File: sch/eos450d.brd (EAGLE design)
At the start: 100 x 80 mm, 19 parts, among them IC1 ATTINY13V, IC2 74HC595, Q1 MMBT2222

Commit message: Schematic complete. Added Gerber files
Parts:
- removed IC1: ATTINY13V, SparkFun-DigitalIC:SO08
- added ISP1: AVRISP-6, adafruit:AVRISP
- added U1: Tiny45-20-SMT, SparkFun-DigitalIC:SO08-EIAJ
- R1, R2: value 51 -> 330
- R3, R4: value 5.6k -> 10k
- R5: value 4.7k -> 3.3k
- R6: value 100 -> 180
- moved C1 80.5 mm to (9.61, 6.53), turned to 90 degrees
- moved R3 69.1 mm to (15.9, 12.1), turned to 180 degrees
- moved R5 67.8 mm to (16.9, 25.9), flipped to the bottom, turned to 90 degrees
- moved S1 67.3 mm to (15.8, 4.99), turned to 90 degrees
- moved C3 65.9 mm to (15.9, 10.1), turned to 180 degrees
- moved S2 64.8 mm to (3.56, 5.08), turned to 270 degrees
- moved C5 64.4 mm to (3.76, 29.5), flipped to the bottom, turned to 90 degrees
- moved R4 63.2 mm to (3.48, 12.1)
- moved Q1 62.7 mm to (16.0, 31.5), flipped to the bottom
- moved C4 61.8 mm to (3.50, 10.1)
- moved R6 55.3 mm to (9.54, 60.1), flipped to the bottom, turned to 180 degrees
- moved R1 52.4 mm to (2.99, 41.1), flipped to the bottom, turned to 180 degrees
- moved D2 47.6 mm to (9.61, 47.5)
- moved C2 38.9 mm to (15.4, 42.1), flipped to the bottom, turned to 270 degrees
- moved BAT1 38.7 mm to (9.58, 23.4), turned to 270 degrees
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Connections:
- removed net N$4: Q1.C, R6.1
- new net N$3: D1.C, Q1.C
- net BTN_PUSH: now also ISP1.5, U1.1; no longer IC1.1
- net BUTTON: now also U1.2; no longer IC1.2
- net CLK: now also ISP1.3, U1.7; no longer IC1.7
- net DATA_IN: now also ISP1.4, U1.5; no longer IC1.5
- net GND: now also ISP1.6, Q1.E, U1.4; no longer D1.C, IC1.4
- net IRLED: now also U1.3; no longer IC1.3
- net LATCH: now also ISP1.1, U1.6; no longer IC1.6
- net N$1: now also R6.1; no longer Q1.E
- net VCC: now also ISP1.2, U1.8; no longer IC1.8
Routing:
- net VCC: track 0.00 -> 93.4 mm, vias 0 -> 2
- net LATCH: track 0.00 -> 77.5 mm, vias 0 -> 1
- net DATA_IN: track 0.00 -> 61.3 mm, vias 0 -> 1
- net CLK: track 0.00 -> 51.0 mm, vias 0 -> 2
- net BTN_PUSH: track 0.00 -> 38.1 mm, vias 0 -> 1
- net N$3: track 0.00 -> 35.1 mm
- net BUTTON: track 0.00 -> 31.7 mm, vias 0 -> 1
- net QH: track 0.00 -> 20.9 mm, vias 0 -> 2
- net QA: track 0.00 -> 14.1 mm
- net QB: track 0.00 -> 13.4 mm
- net DP: track 0.00 -> 12.7 mm
- net C: track 0.00 -> 11.0 mm
- net QE: track 0.00 -> 8.70 mm
- net QF: track 0.00 -> 7.96 mm
- net QD: track 0.00 -> 6.95 mm
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- added copper zone on layer 1, net GND
- added copper zone on layer 16, net GND
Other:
- board size 100 x 80 mm -> 19.2 x 64 mm

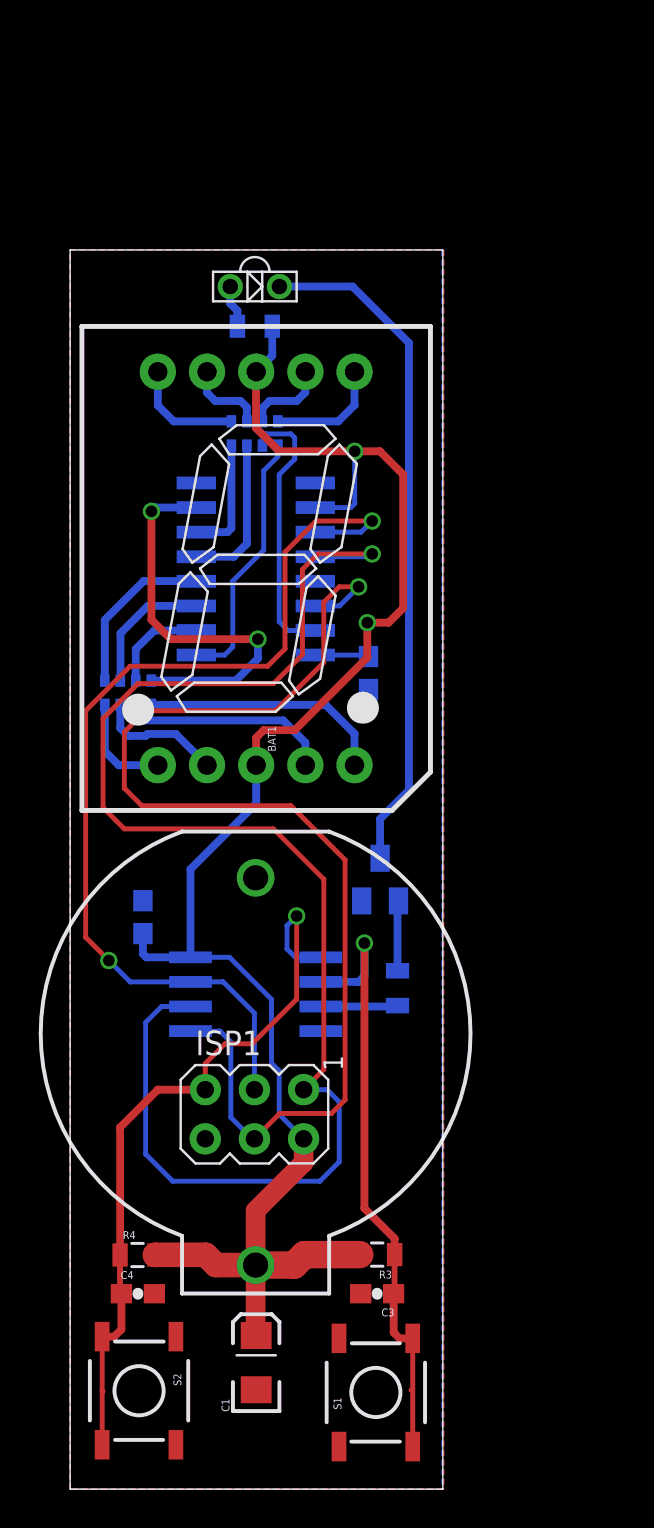
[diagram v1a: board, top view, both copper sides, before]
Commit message: Schematic updated: Auto power switching added
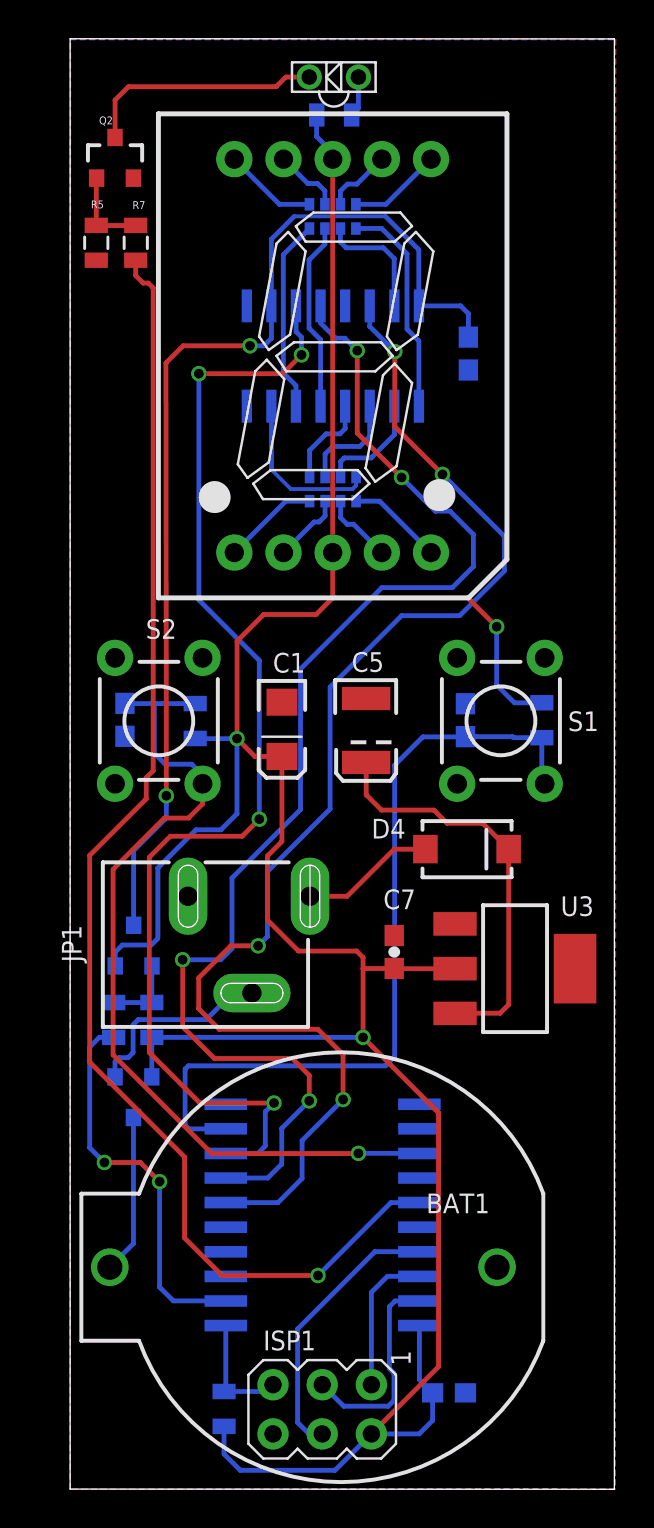
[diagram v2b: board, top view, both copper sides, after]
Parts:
- removed IC2: 74HC595, 74xx-us:SO16
- added C6, C7: 0.1uF, SparkFun-Capacitors:0603-CAP
- added D4: B340A, SparkFun-DiscreteSemi:SMA-DIODE
- added JP1: 9V, SparkFun-Connectors:POWER_JACK_SLOT
- added Q2: PMV20XN/MGSF2N02ELT1G, mine-mosfet:SOT23-3
- added R10: 1M, SparkFun-Passives:0805
- added R7, R9: 150, SparkFun-Passives:0805
- added R8: 1k, SparkFun-Passives:0805
- added U2: ATTINY2313A, SparkFun-DigitalIC:SOP20W
- added U3: 331A, SparkFun-PowerIC:SOT223
- added U4: ZXMP6A13FTA, mine-mosfet:SOT23-3
- C5: value 0.1uF -> 47uF; device SparkFun-Capacitors:0603-CAP -> SparkFun-Capacitors:EIA3528
- Q1: value MMBT2222 -> PMV48XP; device transistor-neu-to92:SOT23-BEC -> mine-mosfet:SOT23-3
- R5: value 3.3k -> 1M
- S1, S2: device SparkFun-Electromechanical:TACTILE-SWITCH-SMD -> SparkFun-Electromechanical:TACTILE-PTH-EZ
- U1: value Tiny45-20-SMT -> 74HC595; device SparkFun-DigitalIC:SO08-EIAJ -> mine-mosfet:SOIC127P600X175-16N
- moved R5 41.5 mm to (1.35, 64.4), flipped to the top
- moved S1 35.3 mm to (22.2, 39.7)
- moved R4 34.6 mm to (24.4, 39.7), flipped to the bottom, turned to 90 degrees
- moved S2 34.6 mm to (4.58, 39.7), turned to 90 degrees
- moved C4 34.1 mm to (20.4, 39.7), flipped to the bottom, turned to 90 degrees
- moved U1 33.2 mm to (13.6, 58.5), turned to 90 degrees
- moved C1 32.7 mm to (10.9, 39.2), turned to 270 degrees
- moved C3 32.4 mm to (2.83, 39.7), flipped to the bottom, turned to 270 degrees
- moved R3 29.1 mm to (6.46, 39.7), flipped to the bottom, turned to 270 degrees
- moved C2 17.3 mm to (20.6, 58.6)
- moved ISP1 15.6 mm to (13.0, 4.12)
- moved C5 15.0 mm to (15.3, 39.2), flipped to the top, turned to 270 degrees
- moved R1 14.9 mm to (13.6, 51.6)
- moved Q1 13.2 mm to (3.28, 28.0)
- moved BAT1 12.7 mm to (13.9, 11.5), turned to 180 degrees
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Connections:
- new net MISO: ISP1.1, U2.18
- new net MOSI: ISP1.4, U2.17
- new net N$10: D4.A, JP1.PWR
- new net N$11: BAT1.1, U4.3
- new net N$12: JP1.GND@2, U4.1
- new net N$4: Q1.1, R10.1, R9.2
- new net N$5: C2.1, Q1.3, U1.10, U1.16
- new net N$6: C5.A, D4.C, U3.3
- new net N$7: ISP1.5, R8.1, U2.1
- new net SCK: ISP1.3, U2.19
- new net TON_SHREG: R9.1, U2.2
- net BTN_PUSH: now also S1.3, U2.9; no longer ISP1.5, S2.3, S2.4, U1.1
- net BUTTON: now also S2.3, U2.13; no longer S1.3, S1.4, U1.2
- net CLK: now also U1.11, U2.8; no longer IC2.11, ISP1.3, U1.7
- net DATA_IN: now also U1.14, U2.6; no longer IC2.14, ISP1.4, U1.5
- net GND: now also C5.C, C6.2, C7.2, JP1.GND@1, Q2.2, R5.1, U1.13, U1.8, U3.1; no longer C5.2, IC2.13, IC2.8, Q1.E, S1.2, S2.2, U1.4
- net IRLED: now also R7.2, U2.15; no longer R5.1, U1.3
- net LATCH: now also U1.12, U2.7; no longer IC2.12, ISP1.1, U1.6
- net N$2: now also Q2.1, R7.1; no longer Q1.B
- net N$3: now also Q2.3; no longer Q1.C
- net QA: now also U1.15; no longer IC2.15
- net QB: now also U1.1; no longer IC2.1
- net QC: now also U1.2; no longer IC2.2
- net QD: now also U1.3; no longer IC2.3
- net QE: now also U1.4; no longer IC2.4
- net QF: now also U1.5; no longer IC2.5
- net QG: now also U1.6; no longer IC2.6
- net QH: now also U1.7; no longer IC2.7
- net VCC: now also C6.1, C7.1, Q1.2, R10.2, R8.2, U2.20, U3.2, U4.2; no longer BAT1.1, C2.1, C5.1, IC2.10, IC2.16, U1.8
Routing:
- net IRLED: track 3.98 -> 68.9 mm, vias 0 -> 1
- net VCC: track 93.4 -> 150.5 mm, vias 2 -> 3
- net N$5: track 0.00 -> 56.9 mm, vias 0 -> 2
- net N$3: track 35.1 -> 12.5 mm
- net N$6: track 0.00 -> 21.2 mm
- net TON_SHREG: track 0.00 -> 20.1 mm, vias 0 -> 2
- net MOSI: track 0.00 -> 14.3 mm
- net BUTTON: track 31.7 -> 44.2 mm
- net QH: track 20.9 -> 8.58 mm, vias 2 -> 0
- net SCK: track 0.00 -> 10.9 mm
- net LATCH: track 77.5 -> 66.7 mm, vias 1 -> 4
- net CLK: track 51.0 -> 61.4 mm, vias 2 -> 4
- net N$12: track 0.00 -> 10.2 mm
- net N$11: track 0.00 -> 8.24 mm
- net QA: track 14.1 -> 6.27 mm
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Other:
- board size 19.2 x 64 mm -> 28.1 x 74.9 mm
- board text added: "CANON EOS TIMELAPSE CONTROLLER v1.0"
- board text added: "D.GOROHOV @2015 DC: 7V-12V"
